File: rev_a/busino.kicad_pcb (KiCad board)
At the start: 2 copper layers, 100 x 100 mm, 50 parts, among them J1 TERMINATE_JUMPER, SW1 2_LEAD_PUSH_BUTTON, U1 VOLTAGE_REGULATOR, U2 MCP2562, U3 VOLTAGE_REGULATOR, U4 74x06, U5 ATMEGA324_DIP40, X1 16MHz

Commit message: Worked on board.
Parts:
- C1, C2, C3, C4, C5, C6, C7: footprint Capacitors_ThroughHole:Capacitor3MMDiscRM2.5 -> Busino_Rev_A:Capacitor3MMDiscRM2.5
- D1: footprint Diodes_ThroughHole:Diode_DO-41_SOD81_Horizontal_RM10 -> Busino_Rev_A:Diode_DO-41_SOD81_Horizontal_RM10
- H1, H10, H11, H12, H2, H3, H4, H5, H6, H7, H8, H9: footprint Mounting_Holes:MountingHole_3mm -> Busino_Rev_A:MountingHole_3mm
- J1: footprint Pin_Headers:Pin_Header_Straight_1x03 -> Busino_Rev_A:Pin_Header_Straight_1x03
- N1: footprint Pin_Headers:Pin_Header_Straight_2x03 -> Busino_Rev_A:Pin_Header_Straight_2x03
- N10: value MS_DATA_HEADER -> MS_SE_DATA_HEADER; footprint Pin_Headers:Pin_Header_Straight_2x08 -> Busino_Rev_A:Pin_Header_Straight_2x08
- N11: value MS_PWR_HEADER -> MS_SEPWR_HEADER; footprint Pin_Headers:Pin_Header_Straight_2x08 -> Busino_Rev_A:Pin_Header_Straight_2x08
- N12: value MS_DATA_HEADER -> MS_NW_DATA_HEADER; footprint Pin_Headers:Pin_Header_Straight_2x08 -> Busino_Rev_A:Pin_Header_Straight_2x08
- N13: value MS_PWR_HEADER -> MS_NW_PWR_HEADER; footprint Pin_Headers:Pin_Header_Straight_2x08 -> Busino_Rev_A:Pin_Header_Straight_2x08
- N14: value MS_DATA_HEADER -> MS_NE_DATA_HEADER; footprint Pin_Headers:Pin_Header_Straight_2x08 -> Busino_Rev_A:Pin_Header_Straight_2x08
- N15: value MS_PWR_HEADER -> MS_NE_PWR_HEADER; footprint Pin_Headers:Pin_Header_Straight_2x08 -> Busino_Rev_A:Pin_Header_Straight_2x08
- N2, N3: footprint Pin_Headers:Pin_Header_Straight_1x08 -> Busino_Rev_A:Pin_Header_Straight_1x08
- N4, N9: footprint Pin_Headers:Pin_Header_Straight_1x06 -> Busino_Rev_A:Pin_Header_Straight_1x06
- N5: footprint Pin_Headers:Pin_Header_Straight_1x06 -> Busino_Rev_A:Pin_Header_Straight_1x08
- N6: value MS_DATA_HEADER -> MS_SW_DATA_HEADER; footprint Pin_Headers:Pin_Header_Straight_2x08 -> Busino_Rev_A:Pin_Header_Straight_2x08
- N7: value MS_PWR_HEADER -> MS_SW_PWR_HEADER; footprint Pin_Headers:Pin_Header_Straight_2x08 -> Busino_Rev_A:Pin_Header_Straight_2x08
- N8: footprint Pin_Headers:Pin_Header_Straight_2x05 -> Busino_Rev_A:Pin_Header_Straight_2x05_Shrouded
- R1, R4, R5, R6, R7: footprint Resistors_ThroughHole:Resistor_Horizontal_RM30mm -> Busino_Rev_A:Resistor_Horizontal__400
- R2, R3: value R_HORIZ -> 1K; footprint Resistors_ThroughHole:Resistor_Horizontal_RM30mm -> Busino_Rev_A:Resistor_Horizontal__400
- U1, U3: footprint Transistors_TO-220:TO-220_Bipolar-BCE_Horizontal_LargePads -> Busino_Rev_A:Regulator_TO_220_Horizontal
- U2: footprint Sockets_DIP:DIP-8__300 -> Busino_Rev_A:DIP-8__300
- U4: footprint Sockets_DIP:DIP-14__300 -> Busino_Rev_A:DIP-14__300
- U5: footprint Sockets_DIP:DIP-40__600 -> Busino_Rev_A:DIP-40__600
- X1: footprint Crystals:Crystal_HC49-U_Vertical -> Busino_Rev_A:Crystal_HC49-U_Vertical
- moved N13 215.8 mm to (31.8, 38.1), turned to 90 degrees
- moved N12 165.6 mm to (69.8, 38.1), turned to 90 degrees
- moved N14 161.2 mm to (120.7, 38.1), turned to 90 degrees
- moved R2 143.4 mm to (111.1, 49.5), turned to 90 degrees
- moved N5 138.6 mm to (57.1, 100.3), turned to 180 degrees
- moved R7 137.4 mm to (142.9, 52.6), turned to 180 degrees
- moved U1 126.5 mm to (107.2, 56.1), turned to 90 degrees
- moved X1 120.7 mm to (56.5, 92.1), turned to 270 degrees
- moved R6 119.5 mm to (143.4, 83.3)
- moved R3 119.3 mm to (114.3, 49.5), turned to 90 degrees
- moved N9 118.2 mm to (121.9, 57.8), turned to 270 degrees
- moved SW1 113.4 mm to (121.9, 99.1), turned to 90 degrees
- moved R4 112.4 mm to (132.1, 48.9), turned to 270 degrees
- moved R1 111.3 mm to (142.9, 90.2), turned to 180 degrees
- moved N15 105.8 mm to (82.5, 38.1), turned to 90 degrees
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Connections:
- N10 pad 10: /Arduino Shield/A4 -> /Arduino Shield/D9
- N10 pad 11: /Arduino Shield/D5 -> /Arduino Shield/D10
- N10 pad 12: /Arduino Shield/A5 -> /Arduino Shield/D11
- N10 pad 13: /Arduino Shield/D6 -> /Arduino Shield/D12
- N10 pad 14: /Arduino Shield/MPWR -> /Arduino Shield/D13
- N10 pad 15: /Arduino Shield/D7 -> /Arduino Shield/MPWR
- N10 pad 2: /Arduino Shield/A0 -> /Arduino Shield/D1
- N10 pad 3: /Arduino Shield/D1 -> /Arduino Shield/D2
- N10 pad 4: /Arduino Shield/A1 -> /Arduino Shield/D3
- N10 pad 5: /Arduino Shield/D2 -> /Arduino Shield/D4
- N10 pad 6: /Arduino Shield/A2 -> /Arduino Shield/D5
- N10 pad 7: /Arduino Shield/D3 -> /Arduino Shield/D6
- N10 pad 8: /Arduino Shield/A3 -> /Arduino Shield/D7
- N10 pad 9: /Arduino Shield/D4 -> /Arduino Shield/D8
- N11 pad 1: /Arduino Shield/D8 -> /Arduino Shield/VIN
- N11 pad 10: +3.3V -> /Arduino Shield/A1
- N11 pad 11: /Arduino Shield/D13 -> /Arduino Shield/A2
- N11 pad 12: /Arduino Shield/~RESET -> /Arduino Shield/A3
- N11 pad 13: /Arduino Shield/VIN -> /Arduino Shield/A4
- N11 pad 14: /Arduino Shield/MGND -> /Arduino Shield/A5
- N11 pad 15: /Arduino Shield/AREF -> /Arduino Shield/MGND
- N11 pad 3: /Arduino Shield/D9 -> +5V
- N11 pad 4: GND -> +3.3V
- N11 pad 5: /Arduino Shield/D10 -> GND
- N11 pad 7: /Arduino Shield/D11 -> /Arduino Shield/AREF
- N11 pad 8: +5V -> /Arduino Shield/~RESET
- N11 pad 9: /Arduino Shield/D12 -> /Arduino Shield/A0
- N12 pad 10: /Arduino Shield/A4 -> /Arduino Shield/D9
- N12 pad 11: /Arduino Shield/D5 -> /Arduino Shield/D10
- N12 pad 12: /Arduino Shield/A5 -> /Arduino Shield/D11
- N12 pad 13: /Arduino Shield/D6 -> /Arduino Shield/D12
- N12 pad 14: /Arduino Shield/MPWR -> /Arduino Shield/D13
- N12 pad 15: /Arduino Shield/D7 -> /Arduino Shield/MPWR
- N12 pad 2: /Arduino Shield/A0 -> /Arduino Shield/D1
- N12 pad 3: /Arduino Shield/D1 -> /Arduino Shield/D2
- N12 pad 4: /Arduino Shield/A1 -> /Arduino Shield/D3
- N12 pad 5: /Arduino Shield/D2 -> /Arduino Shield/D4
- N12 pad 6: /Arduino Shield/A2 -> /Arduino Shield/D5
- N12 pad 7: /Arduino Shield/D3 -> /Arduino Shield/D6
- N12 pad 8: /Arduino Shield/A3 -> /Arduino Shield/D7
- N12 pad 9: /Arduino Shield/D4 -> /Arduino Shield/D8
- N13 pad 1: /Arduino Shield/D8 -> /Arduino Shield/VIN
- N13 pad 10: +3.3V -> /Arduino Shield/A1
- N13 pad 11: /Arduino Shield/D13 -> /Arduino Shield/A2
- N13 pad 12: /Arduino Shield/~RESET -> /Arduino Shield/A3
- N13 pad 13: /Arduino Shield/VIN -> /Arduino Shield/A4
- N13 pad 14: /Arduino Shield/MGND -> /Arduino Shield/A5
- N13 pad 15: /Arduino Shield/AREF -> /Arduino Shield/MGND
- N13 pad 3: /Arduino Shield/D9 -> +5V
- N13 pad 4: GND -> +3.3V
- N13 pad 5: /Arduino Shield/D10 -> GND
- N13 pad 7: /Arduino Shield/D11 -> /Arduino Shield/AREF
- N13 pad 8: +5V -> /Arduino Shield/~RESET
- N13 pad 9: /Arduino Shield/D12 -> /Arduino Shield/A0
- N14 pad 10: /Arduino Shield/A4 -> /Arduino Shield/D9
- N14 pad 11: /Arduino Shield/D5 -> /Arduino Shield/D10
- N14 pad 12: /Arduino Shield/A5 -> /Arduino Shield/D11
- N14 pad 13: /Arduino Shield/D6 -> /Arduino Shield/D12
- N14 pad 14: /Arduino Shield/MPWR -> /Arduino Shield/D13
- N14 pad 15: /Arduino Shield/D7 -> /Arduino Shield/MPWR
- N14 pad 2: /Arduino Shield/A0 -> /Arduino Shield/D1
- N14 pad 3: /Arduino Shield/D1 -> /Arduino Shield/D2
- N14 pad 4: /Arduino Shield/A1 -> /Arduino Shield/D3
- N14 pad 5: /Arduino Shield/D2 -> /Arduino Shield/D4
- N14 pad 6: /Arduino Shield/A2 -> /Arduino Shield/D5
- N14 pad 7: /Arduino Shield/D3 -> /Arduino Shield/D6
- N14 pad 8: /Arduino Shield/A3 -> /Arduino Shield/D7
- N14 pad 9: /Arduino Shield/D4 -> /Arduino Shield/D8
- N15 pad 1: /Arduino Shield/D8 -> /Arduino Shield/VIN
- N15 pad 10: +3.3V -> /Arduino Shield/A1
- N15 pad 11: /Arduino Shield/D13 -> /Arduino Shield/A2
- N15 pad 12: /Arduino Shield/~RESET -> /Arduino Shield/A3
- N15 pad 13: /Arduino Shield/VIN -> /Arduino Shield/A4
- N15 pad 14: /Arduino Shield/MGND -> /Arduino Shield/A5
- N15 pad 15: /Arduino Shield/AREF -> /Arduino Shield/MGND
- N15 pad 3: /Arduino Shield/D9 -> +5V
- N15 pad 4: GND -> +3.3V
- N15 pad 5: /Arduino Shield/D10 -> GND
- N15 pad 7: /Arduino Shield/D11 -> /Arduino Shield/AREF
- N15 pad 8: +5V -> /Arduino Shield/~RESET
- N15 pad 9: /Arduino Shield/D12 -> /Arduino Shield/A0
- N6 pad 10: /Arduino Shield/A4 -> /Arduino Shield/D9
- N6 pad 11: /Arduino Shield/D5 -> /Arduino Shield/D10
- N6 pad 12: /Arduino Shield/A5 -> /Arduino Shield/D11
- N6 pad 13: /Arduino Shield/D6 -> /Arduino Shield/D12
- N6 pad 14: /Arduino Shield/MPWR -> /Arduino Shield/D13
- N6 pad 15: /Arduino Shield/D7 -> /Arduino Shield/MPWR
- N6 pad 2: /Arduino Shield/A0 -> /Arduino Shield/D1
- N6 pad 3: /Arduino Shield/D1 -> /Arduino Shield/D2
- N6 pad 4: /Arduino Shield/A1 -> /Arduino Shield/D3
- N6 pad 5: /Arduino Shield/D2 -> /Arduino Shield/D4
- N6 pad 6: /Arduino Shield/A2 -> /Arduino Shield/D5
- N6 pad 7: /Arduino Shield/D3 -> /Arduino Shield/D6
- N6 pad 8: /Arduino Shield/A3 -> /Arduino Shield/D7
- N6 pad 9: /Arduino Shield/D4 -> /Arduino Shield/D8
- N7 pad 1: /Arduino Shield/D8 -> /Arduino Shield/VIN
- N7 pad 10: +3.3V -> /Arduino Shield/A1
- N7 pad 11: /Arduino Shield/D13 -> /Arduino Shield/A2
- N7 pad 12: /Arduino Shield/~RESET -> /Arduino Shield/A3
- N7 pad 13: /Arduino Shield/VIN -> /Arduino Shield/A4
- N7 pad 14: /Arduino Shield/MGND -> /Arduino Shield/A5
- N7 pad 15: /Arduino Shield/AREF -> /Arduino Shield/MGND
- N7 pad 3: /Arduino Shield/D9 -> +5V
- N7 pad 4: GND -> +3.3V
- N7 pad 5: /Arduino Shield/D10 -> GND
- N7 pad 7: /Arduino Shield/D11 -> /Arduino Shield/AREF
- N7 pad 8: +5V -> /Arduino Shield/~RESET
- N7 pad 9: /Arduino Shield/D12 -> /Arduino Shield/A0
- R2 pad 2: Net-(R2-Pad2) -> /Arduino Shield/D1
- R3 pad 2: Net-(R3-Pad2) -> /Arduino Shield/D0
- U2 pad 1: Net-(R3-Pad2) -> Net-(U2-Pad1)
- U2 pad 4: Net-(R2-Pad2) -> Net-(U2-Pad4)
- U4 pad 1: Net-(R3-Pad2) -> Net-(U2-Pad1)
- U5 pad 16: Net-(R3-Pad2) -> Net-(U2-Pad1)
- U5 pad 17: Net-(R2-Pad2) -> Net-(U2-Pad4)
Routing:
- net /Arduino Shield/D9: track 0.00 -> 332.3 mm, vias 0 -> 5
- net /Arduino Shield/MPWR: track 0.00 -> 329.5 mm, vias 0 -> 1
- net /Arduino Shield/~RESET: track 0.00 -> 293.1 mm, vias 0 -> 4
- net /Arduino Shield/D5: track 0.00 -> 288.1 mm, vias 0 -> 5
- net /Arduino Shield/A2: track 0.00 -> 268.8 mm, vias 0 -> 7
- net /Arduino Shield/A1: track 0.00 -> 268.2 mm, vias 0 -> 4
- net /Arduino Shield/D6: track 0.00 -> 268.2 mm, vias 0 -> 6
- net /Arduino Shield/MGND: track 0.00 -> 267.0 mm
- net /Arduino Shield/D11: track 0.00 -> 263.2 mm, vias 0 -> 6
- net /Arduino Shield/D12: track 0.00 -> 262.6 mm, vias 0 -> 6
- net /Arduino Shield/A5: track 0.00 -> 259.0 mm, vias 0 -> 4
- net /Arduino Shield/D13: track 0.00 -> 258.0 mm, vias 0 -> 4
- net /Arduino Shield/A3: track 0.00 -> 255.6 mm, vias 0 -> 5
- net /Arduino Shield/A0: track 0.00 -> 254.8 mm, vias 0 -> 5
- net /Arduino Shield/A4: track 0.00 -> 246.5 mm, vias 0 -> 3
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- added copper zone on B.Cu, net GND
- added copper zone on F.Cu, net GND
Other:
- net class Power added: clearance 0.254, trace_width 1.016, via_dia 1.016, via_drill 0.635

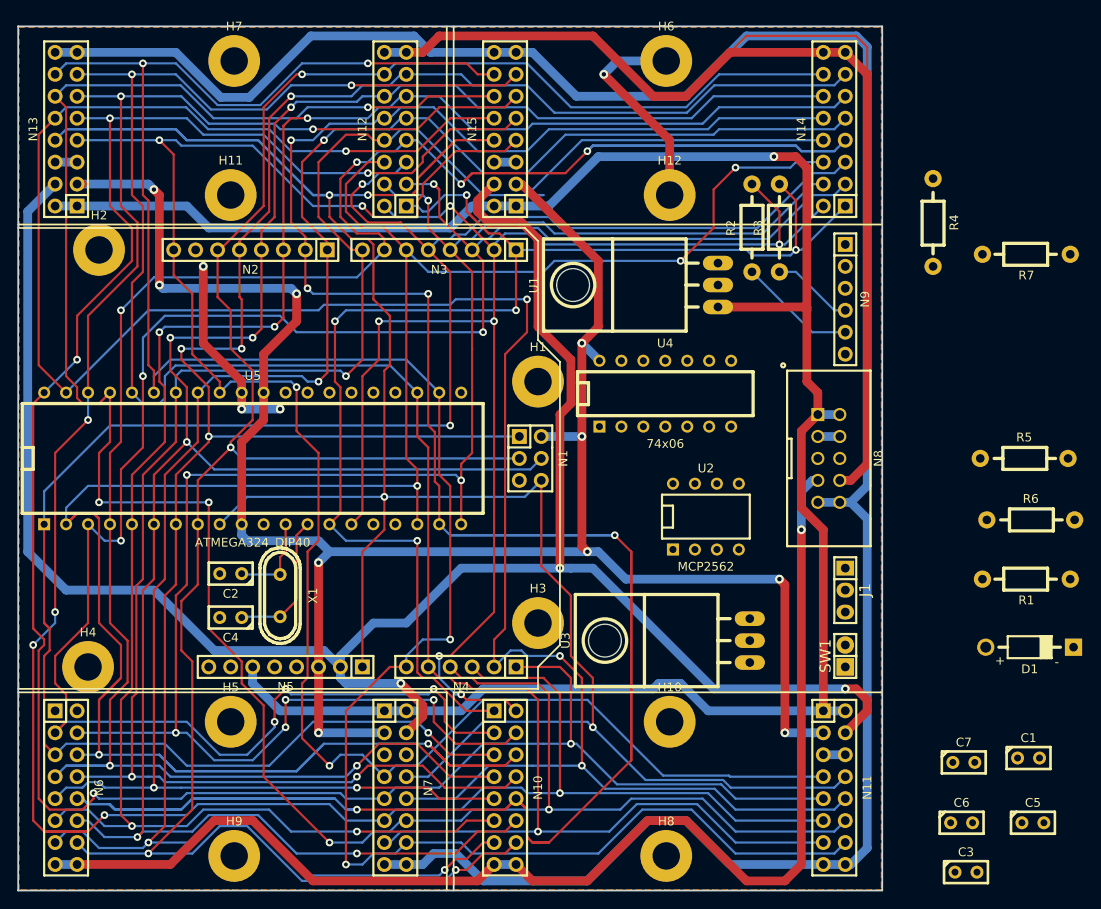
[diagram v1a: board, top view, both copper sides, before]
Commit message: Busino passes DRC.
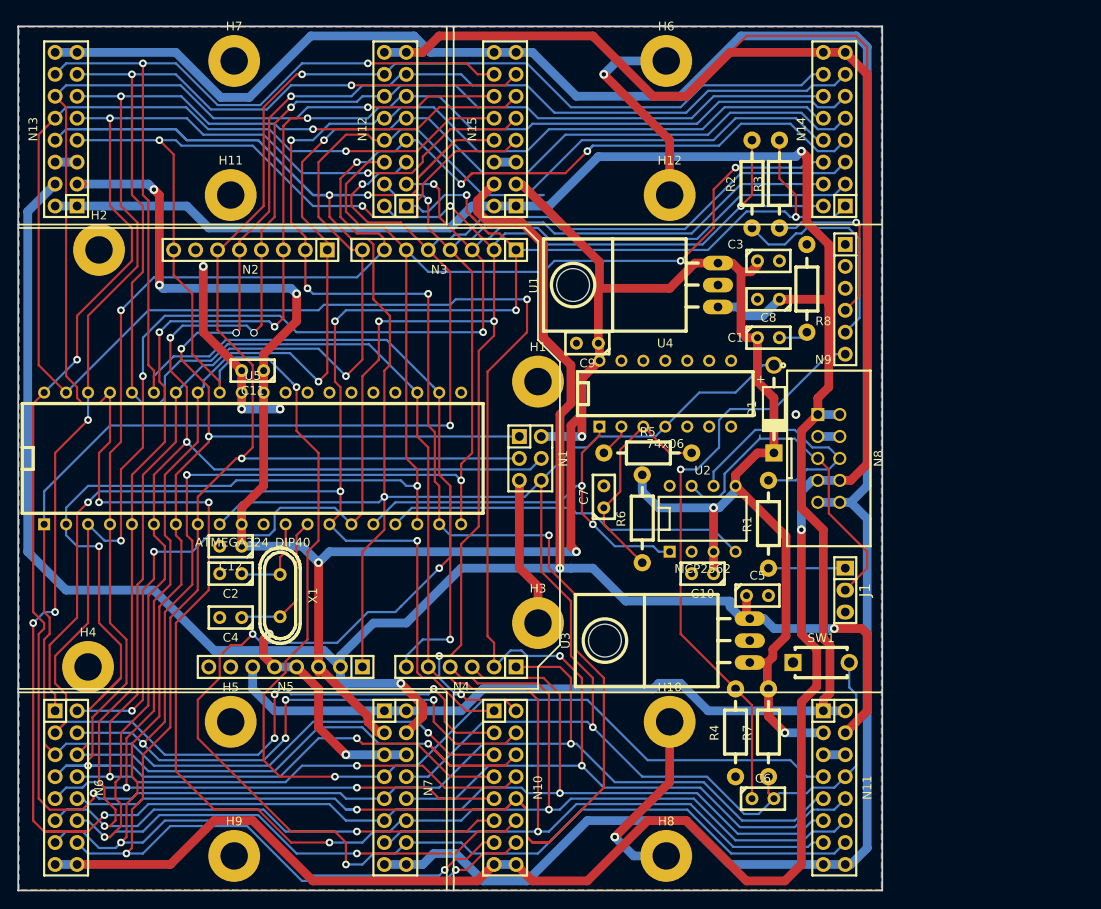
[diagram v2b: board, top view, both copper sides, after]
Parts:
- added C10: .1uF, Busino_Rev_A:Capacitor3MMDiscRM2.5, F.Cu at (105.4, 89.5)
- added C11: .1uF, Busino_Rev_A:Capacitor3MMDiscRM2.5, F.Cu at (53.3, 66.0)
- added C12: .1uF, Busino_Rev_A:Capacitor3MMDiscRM2.5, F.Cu at (50.8, 86.4)
- added C8: .1uF, Busino_Rev_A:Capacitor3MMDiscRM2.5, F.Cu at (113.0, 62.2)
- added C9: .1uF, Busino_Rev_A:Capacitor3MMDiscRM2.5, F.Cu at (92.1, 62.9)
- added R8: .47, Busino_Rev_A:Resistor_Horizontal__400, F.Cu at (117.5, 56.5)
- C1, C3, C5: value .1uF -> 22uF
- SW1: footprint Pin_Headers:Pin_Header_Straight_1x02 -> Busino_Rev_A:BUTTON_6.5MM
- U1: value VOLTAGE_REGULATOR -> LM2940CT-5.0
- U3: value VOLTAGE_REGULATOR -> LM1117T-3.3
- moved C3 74.3 mm to (113.0, 53.3)
- moved R4 63.3 mm to (109.2, 108.0), turned to 90 degrees
- moved R7 62.9 mm to (113.0, 108.0), turned to 90 degrees
- moved C1 61.0 mm to (113.0, 57.8), turned to 180 degrees
- moved C7 51.8 mm to (94.0, 80.6), turned to 90 degrees
- moved R6 45.0 mm to (98.4, 83.2), turned to 90 degrees
- moved R5 43.6 mm to (99.1, 75.6)
- moved C5 41.3 mm to (111.8, 92.1)
- moved D1 40.4 mm to (113.7, 70.5), turned to 270 degrees
- moved R1 30.5 mm to (113.0, 83.8), turned to 90 degrees
- moved C6 23.2 mm to (112.4, 115.6)
- moved R2 5.08 mm to (111.1, 44.5)
- moved R3 5.08 mm to (114.3, 44.5)
- moved SW1 2.90 mm to (119.1, 99.8), turned to 0 degrees
- moved U2 0.46 mm to (105.4, 83.2)
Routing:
- net /Arduino Shield/D9: track 332.3 -> 252.3 mm
- net Net-(C6-Pad1): track 0.00 -> 68.0 mm, vias 0 -> 1
- net GND: track 57.9 -> 124.8 mm, vias 4 -> 7
- net +5V: track 243.2 -> 305.5 mm, vias 10 -> 8
- net /Arduino Shield/D0: track 159.9 -> 217.1 mm, vias 5 -> 7
- net /Arduino Shield/D1: track 167.3 -> 219.8 mm, vias 6 -> 8
- net /Arduino Shield/~RESET: track 293.1 -> 344.9 mm
- net /Arduino Shield/A5: track 259.0 -> 309.8 mm, vias 4 -> 6
- net Net-(U2-Pad1): track 0.00 -> 48.8 mm, vias 0 -> 2
- net Net-(U2-Pad4): track 0.00 -> 42.3 mm
- net Net-(J1-Pad2): track 0.00 -> 39.4 mm
- net /Arduino Shield/D5: track 288.1 -> 257.8 mm
- net Net-(N8-Pad6): track 0.00 -> 28.9 mm
- net Net-(C7-Pad1): track 0.00 -> 26.3 mm
- net /Arduino Shield/D6: track 268.2 -> 243.7 mm
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
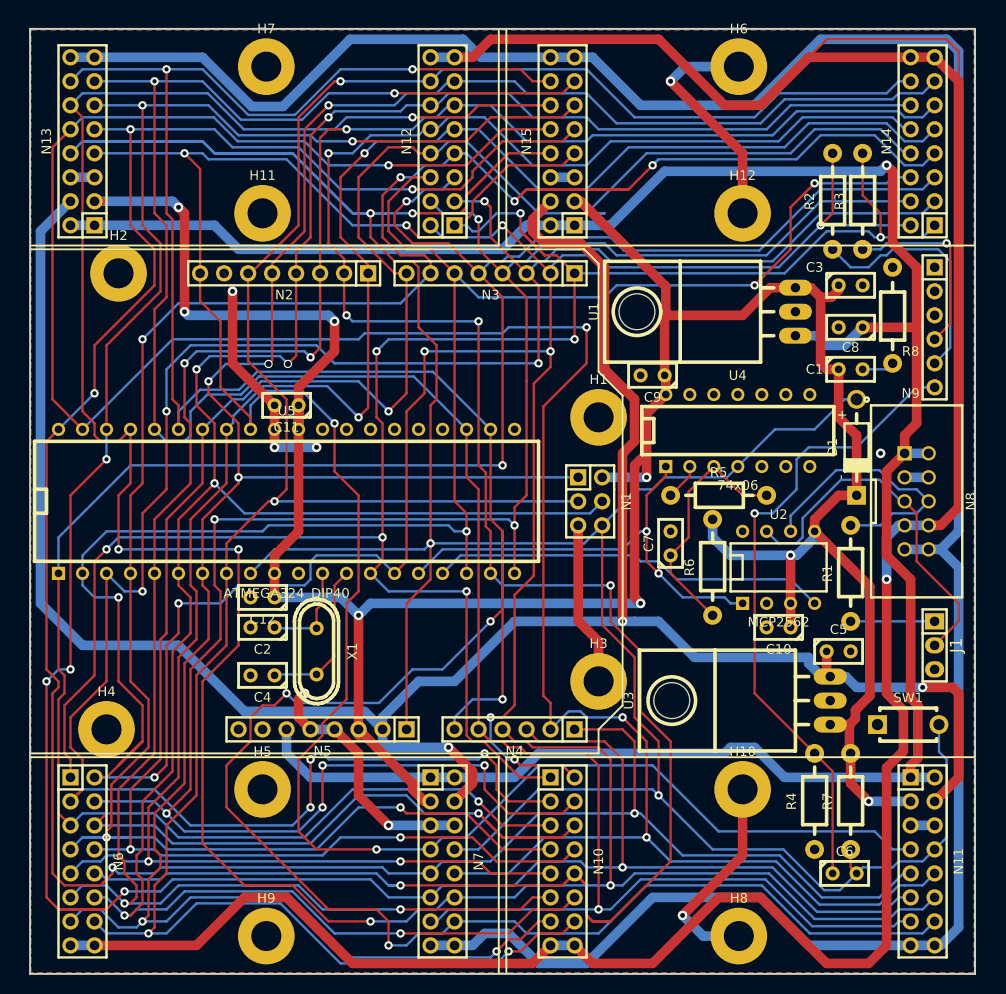
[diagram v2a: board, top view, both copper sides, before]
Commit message: Added more silk screen labels.
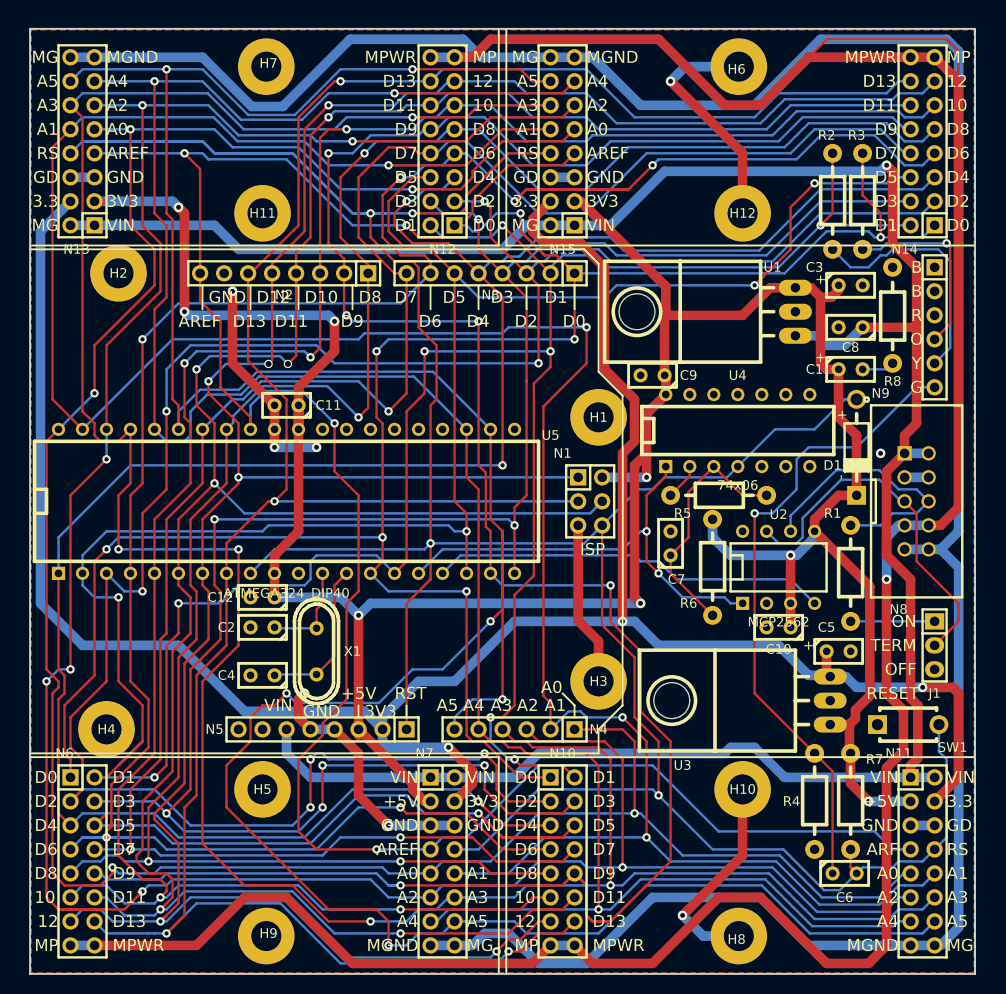
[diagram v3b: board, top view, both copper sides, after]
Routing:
- net /Arduino Shield/A2: track 270.8 -> 275.9 mm
- net /Arduino Shield/D7: track 224.8 -> 221.0 mm
- net /Arduino Shield/D12: track 263.3 -> 265.3 mm
- net /Arduino Shield/D10: track 224.7 -> 225.8 mm
- net /Arduino Shield/D11: track 267.1 -> 268.3 mm
- net /Arduino Shield/D13: track 256.6 -> 255.8 mm
- net +3.3V: track 239.4 -> 239.9 mm
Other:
- board text added: "+"
- board text added: "+5V"
- board text added: "10"
- board text added: "12"
- board text added: "3.3"
- board text added: "3V3"
- board text added: "A0"
- board text added: "A1"
- board text added: "A2"
- board text added: "A3"
- board text added: "A4"
- board text added: "A5"
- board text added: "AREF"
- board text added: "ARF"
- board text added: "B"
- board text added: "D0"
- board text added: "D1"
- board text added: "D10"
- board text added: "D11"
- board text added: "D12"
- board text added: "D13"
- board text added: "D2"
- board text added: "D3"
- board text added: "D4"
- board text added: "D5"
- board text added: "D6"
- board text added: "D7"
- board text added: "D8"
- board text added: "D9"
- board text added: "G"
- board text added: "GD"
- board text added: "GND"
- board text added: "ISP"
- board text added: "MG"
- board text added: "MGND"
- board text added: "MP"
- board text added: "MPWR"
- board text added: "O"
- board text added: "OFF"
- board text added: "ON"
- board text added: "R"
- board text added: "RESET"
- board text added: "RS"
- board text added: "RST"
- board text added: "TERM"
- board text added: "VIN"
- board text added: "Y"

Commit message: Rev. A of the Busino board layout is in pretty good shape.
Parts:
- added D2: LED, Busino_Rev_A:T1_LED, F.Cu at (94.0, 88.3)
- added J2: LED_JUMPER, Busino_Rev_A:Pin_Header_Straight_2x02, F.Cu at (93.3, 81.9)
- added N16: AVR_JTAG_CONNECTOR, Busino_Rev_A:Pin_Header_Straight_2x05_Shrouded, F.Cu at (36.8, 61.0)
- added R10: R_VERT, Busino_Rev_A:Resistor_Horizontal__400, F.Cu at (74.9, 61.0)
- added R9: R_VERT, Busino_Rev_A:Resistor_Horizontal__400, F.Cu at (67.9, 88.9)
- added X2: OSHW_LOGO, Busino_Rev_A:OSHW_LOGO_250mil, F.Cu at (43.2, 95.9)
- N5: footprint Busino_Rev_A:Pin_Header_Straight_1x08 -> Busino_Rev_A:Pin_Header_Straight_1x06
- moved C7 5.12 mm to (94.6, 75.6), turned to 180 degrees
- moved R5 5.08 mm to (104.1, 75.6)
- moved N5 2.54 mm to (59.7, 100.3)
- moved U4 0.18 mm to (101.0, 68.6)
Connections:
- J1 pad 3: Net-(J1-Pad3) -> (no net)
- N1 pad 5: GND -> /Arduino Shield/~RESET
- N1 pad 6: /Arduino Shield/~RESET -> GND
- N9 pad 2: Net-(N9-Pad2) -> (no net)
- N9 pad 3: Net-(N9-Pad3) -> (no net)
- U5 pad 21: Net-(U5-Pad21) -> (no net)
- U5 pad 28: Net-(U5-Pad28) -> (no net)
- U5 pad 29: Net-(U5-Pad29) -> (no net)
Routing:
- net GND: track 124.8 -> 641.1 mm, vias 7 -> 42
- net /Arduino Shield/D5: track 257.8 -> 338.5 mm, vias 5 -> 9
- net /Arduino Shield/MPWR: track 333.5 -> 269.8 mm
- net Net-(N16-Pad1): track 0.00 -> 44.1 mm, vias 0 -> 1
- net Net-(N16-Pad3): track 0.00 -> 43.4 mm, vias 0 -> 2
- net Net-(N16-Pad5): track 0.00 -> 37.3 mm, vias 0 -> 1
- net Net-(J2-Pad1): track 0.00 -> 36.9 mm, vias 0 -> 1
- net /Arduino Shield/D13: track 255.8 -> 292.3 mm, vias 4 -> 5
- net Net-(J2-Pad2): track 0.00 -> 36.0 mm, vias 0 -> 1
- net Net-(N16-Pad9): track 0.00 -> 28.5 mm, vias 0 -> 1
- net /Arduino Shield/D6: track 243.7 -> 262.8 mm
- net /Arduino Shield/D2: track 231.2 -> 245.7 mm, vias 7 -> 9
- net /Arduino Shield/~RESET: track 344.9 -> 358.1 mm, vias 4 -> 5
- net +5V: track 305.5 -> 318.5 mm, vias 8 -> 10
- net /Arduino Shield/A0: track 256.9 -> 268.6 mm
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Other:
- board outline removed
- board text added: "Busino Rev. A 7Jul2014 Copyright (c) 2014 by Gramlich"
- board text added: "D"
- board text added: "JTAG"
- board text added: "Open Source"
- board text added: "P"
- board text added: "hardware"
